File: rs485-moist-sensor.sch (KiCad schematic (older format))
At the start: 26 parts, among them IC1 ATTINY441-MU, P1 CONN_02X03, P2 CONN_01X04, U1 SP3481EN, X1 16MHz

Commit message: Add schematics PDF
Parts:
- R1, R10, R2, R4, R5, R6, R7, R8, R9, TH1: footprint SMD_Packages:SMD-0603_r -> Resistors_SMD:R_0603
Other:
- note added: "Gerai patikrink kojas datasheete:\n* ar geras pinas EXCITATION signalui?\n* ar yra kokių skirtumų tarp USART1 ir USART2?\n"
- note removed: "Gerai patikrink kojas datasheete:\n* kur yra programavimo pinai ir kur spi\n* ar geras pinas EXCITATION signalui?\n* ar yra kokių skirtumų tarp USART1 ir USART2?\n\nBe to:\n* ar lengva rasti 20MHz kristalų?\n* ar darom temperatūros sensorius?"
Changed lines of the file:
@@
 encoding utf-8
 Sheet 1 1
-Title ""
-Date ""
+Title "Digital soil moisture sensor"
+Date "Tue 17 Feb 2015"
 Rev ""
-Comp ""
-Comment1 ""
+Comp "Catnip electronics"
+Comment1 "by Albertas Mickėnas mic@wemakethings.net"
 Comment2 ""
 Comment3 ""
@@
 F 0 "R4" V 8330 3050 50  0000 C CNN
 F 1 "R" V 8257 3051 50  0000 C CNN
-F 2 "SMD_Packages:SMD-0603_r" V 8180 3050 30  0001 C CNN
+F 2 "Resistors_SMD:R_0603" V 8180 3050 30  0001 C CNN
 F 3 "" H 8250 3050 30  0000 C CNN
 	1    8250 3050
@@
 F 0 "R5" V 9380 2100 50  0000 C CNN
 F 1 "1M" V 9307 2101 50  0000 C CNN
-F 2 "SMD_Packages:SMD-0603_r" V 9230 2100 30  0001 C CNN
+F 2 "Resistors_SMD:R_0603" V 9230 2100 30  0001 C CNN
 F 3 "" H 9300 2100 30  0000 C CNN
 	1    9300 2100
@@
 F 0 "R8" V 9680 4050 50  0000 C CNN
 F 1 "1M" V 9607 4051 50  0000 C CNN
-F 2 "SMD_Packages:SMD-0603_r" V 9530 4050 30  0001 C CNN
+F 2 "Resistors_SMD:R_0603" V 9530 4050 30  0001 C CNN
 F 3 "" H 9600 4050 30  0000 C CNN
 	1    9600 4050
@@
 F 0 "R7" V 9680 2600 50  0000 C CNN
 F 1 "1M" V 9607 2601 50  0000 C CNN
-F 2 "SMD_Packages:SMD-0603_r" V 9530 2600 30  0001 C CNN
+F 2 "Resistors_SMD:R_0603" V 9530 2600 30  0001 C CNN
 F 3 "" H 9600 2600 30  0000 C CNN
 	1    9600 2600
@@
 F 0 "R6" V 9380 3550 50  0000 C CNN
 F 1 "1M" V 9307 3551 50  0000 C CNN
-F 2 "SMD_Packages:SMD-0603_r" V 9230 3550 30  0001 C CNN
+F 2 "Resistors_SMD:R_0603" V 9230 3550 30  0001 C CNN
 F 3 "" H 9300 3550 30  0000 C CNN
 	1    9300 3550
@@
 F 0 "R1" V 4730 2900 50  0000 C CNN
 F 1 "10k" V 4657 2901 50  0000 C CNN
-F 2 "SMD_Packages:SMD-0603_r" V 4580 2900 30  0001 C CNN
+F 2 "Resistors_SMD:R_0603" V 4580 2900 30  0001 C CNN
 F 3 "" H 4650 2900 30  0000 C CNN
 	1    4650 2900
@@
 SENSE_LOW
 Text Notes 2450 4900 0    60   ~ 0
-Gerai patikrink kojas datasheete:\n* kur yra programavimo pinai ir kur spi\n* ar geras pinas EXCITATION signalui?\n* ar yra kokių skirtumų tarp USART1 ir USART2?\n\nBe to:\n* ar lengva rasti 20MHz kristalų?\n* ar darom temperatūros sensorius?
+Gerai patikrink kojas datasheete:\n* ar geras pinas EXCITATION signalui?\n* ar yra kokių skirtumų tarp USART1 ir USART2?\n
 $Comp
 L THERMISTOR TH1
@@
 F 0 "TH1" V 7350 4600 50  0000 C CNN
 F 1 "THERMISTOR" V 7150 4550 50  0000 C BNN
-F 2 "SMD_Packages:SMD-0603_r" H 7250 4550 60  0001 C CNN
+F 2 "Resistors_SMD:R_0603" H 7250 4550 60  0001 C CNN
 F 3 "" H 7250 4550 60  0000 C CNN
 	1    7250 4550
@@
 F 0 "R2" V 7330 4050 50  0000 C CNN
 F 1 "10k 0.1%" V 7257 4051 50  0000 C CNN
-F 2 "SMD_Packages:SMD-0603_r" V 7180 4050 30  0001 C CNN
+F 2 "Resistors_SMD:R_0603" V 7180 4050 30  0001 C CNN
 F 3 "" H 7250 4050 30  0000 C CNN
 	1    7250 4050
@@
 F 0 "R9" V 5630 2300 50  0000 C CNN
 F 1 "1k" V 5557 2301 50  0000 C CNN
-F 2 "SMD_Packages:SMD-0603_r" V 5480 2300 30  0001 C CNN
+F 2 "Resistors_SMD:R_0603" V 5480 2300 30  0001 C CNN
 F 3 "" H 5550 2300 30  0000 C CNN
 	1    5550 2300
@@
 F 0 "R10" V 7530 1900 50  0000 C CNN
 F 1 "120" V 7457 1901 50  0000 C CNN
-F 2 "SMD_Packages:SMD-0603_r" V 7380 1900 30  0001 C CNN
+F 2 "Resistors_SMD:R_0603" V 7380 1900 30  0001 C CNN
 F 3 "" H 7450 1900 30  0000 C CNN
 	1    7450 1900

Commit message: Some most recent changes
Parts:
- D1, D2: value DIODESCH -> BAT54
- R4: value R -> 330
- R9: value 1k -> 330
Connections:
- wire segments 42 -> 40
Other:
- moved on the sheet: C1, C2, C3, C4, C5, C6, C7, R10, R2, R4, R5, R6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

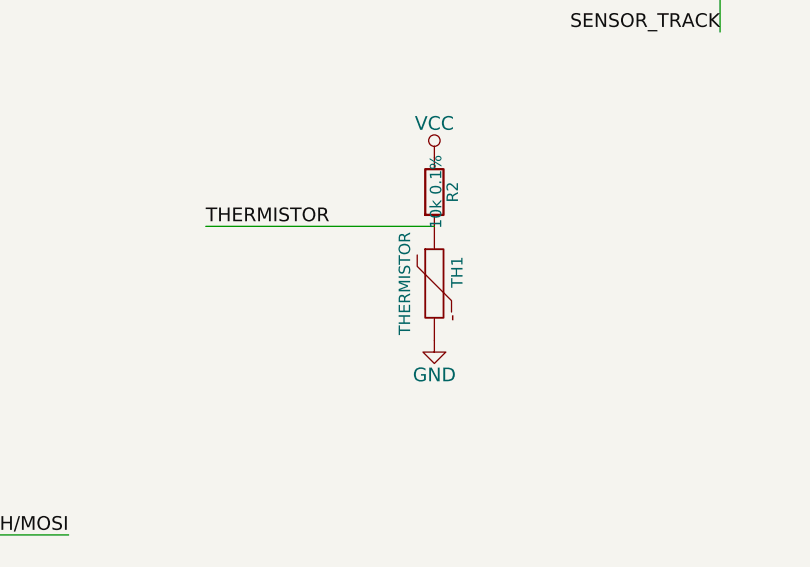
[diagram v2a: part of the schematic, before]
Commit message: Specify thermistor
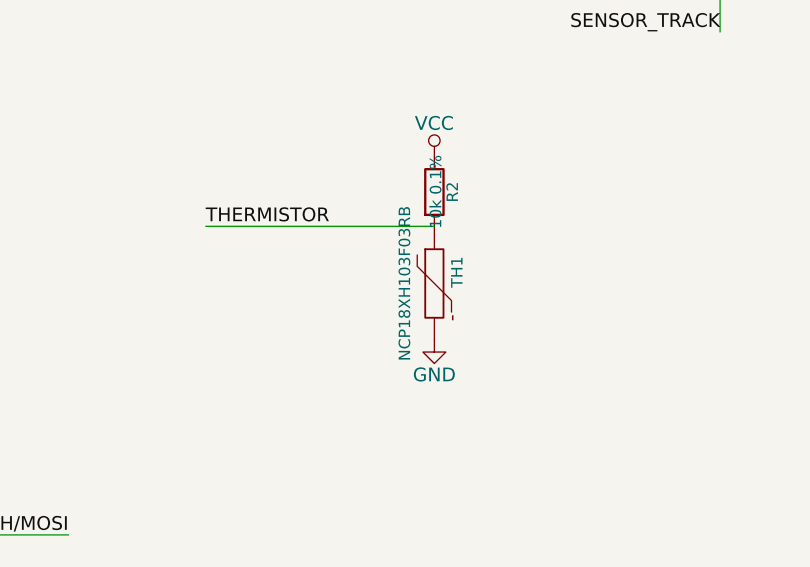
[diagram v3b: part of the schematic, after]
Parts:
- TH1: value THERMISTOR -> NCP18XH103F03RB
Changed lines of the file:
@@
 P 7250 4550
 F 0 "TH1" V 7350 4600 50  0000 C CNN
-F 1 "THERMISTOR" V 7150 4550 50  0000 C BNN
+F 1 "NCP18XH103F03RB" V 7150 4550 50  0000 C BNN
 F 2 "Resistors_SMD:R_0603" H 7250 4550 60  0001 C CNN
 F 3 "" H 7250 4550 60  0000 C CNN

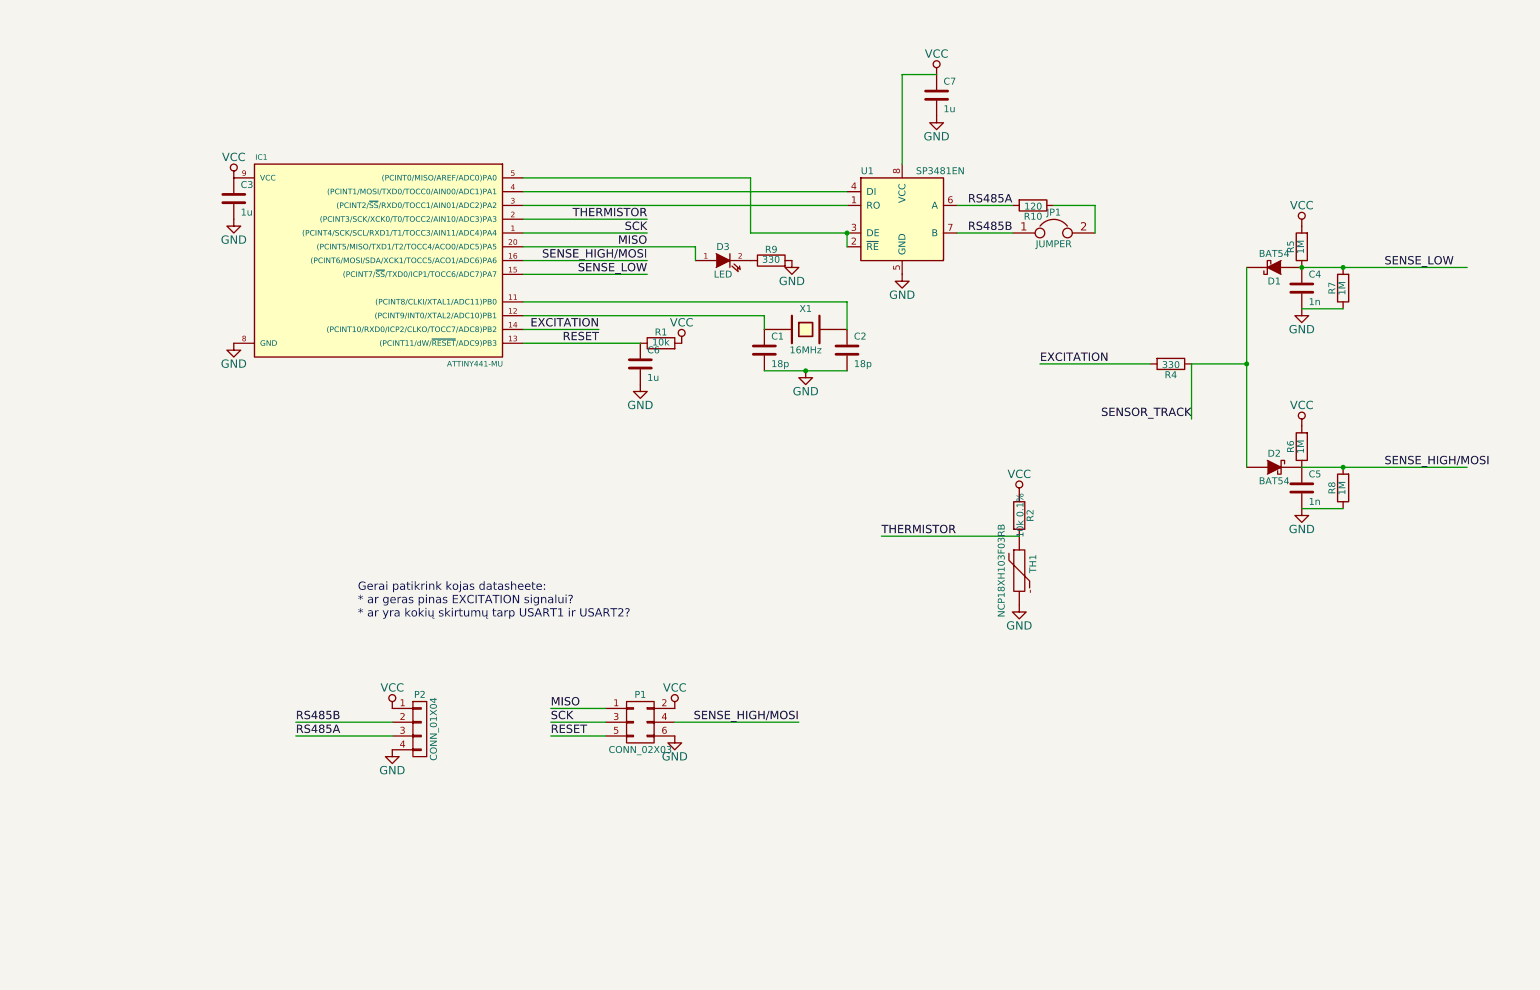
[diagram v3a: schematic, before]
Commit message: Add a local voltage regulator, add antistatic protection, specify transceiver, change attiny441 package to soic-14, route everything
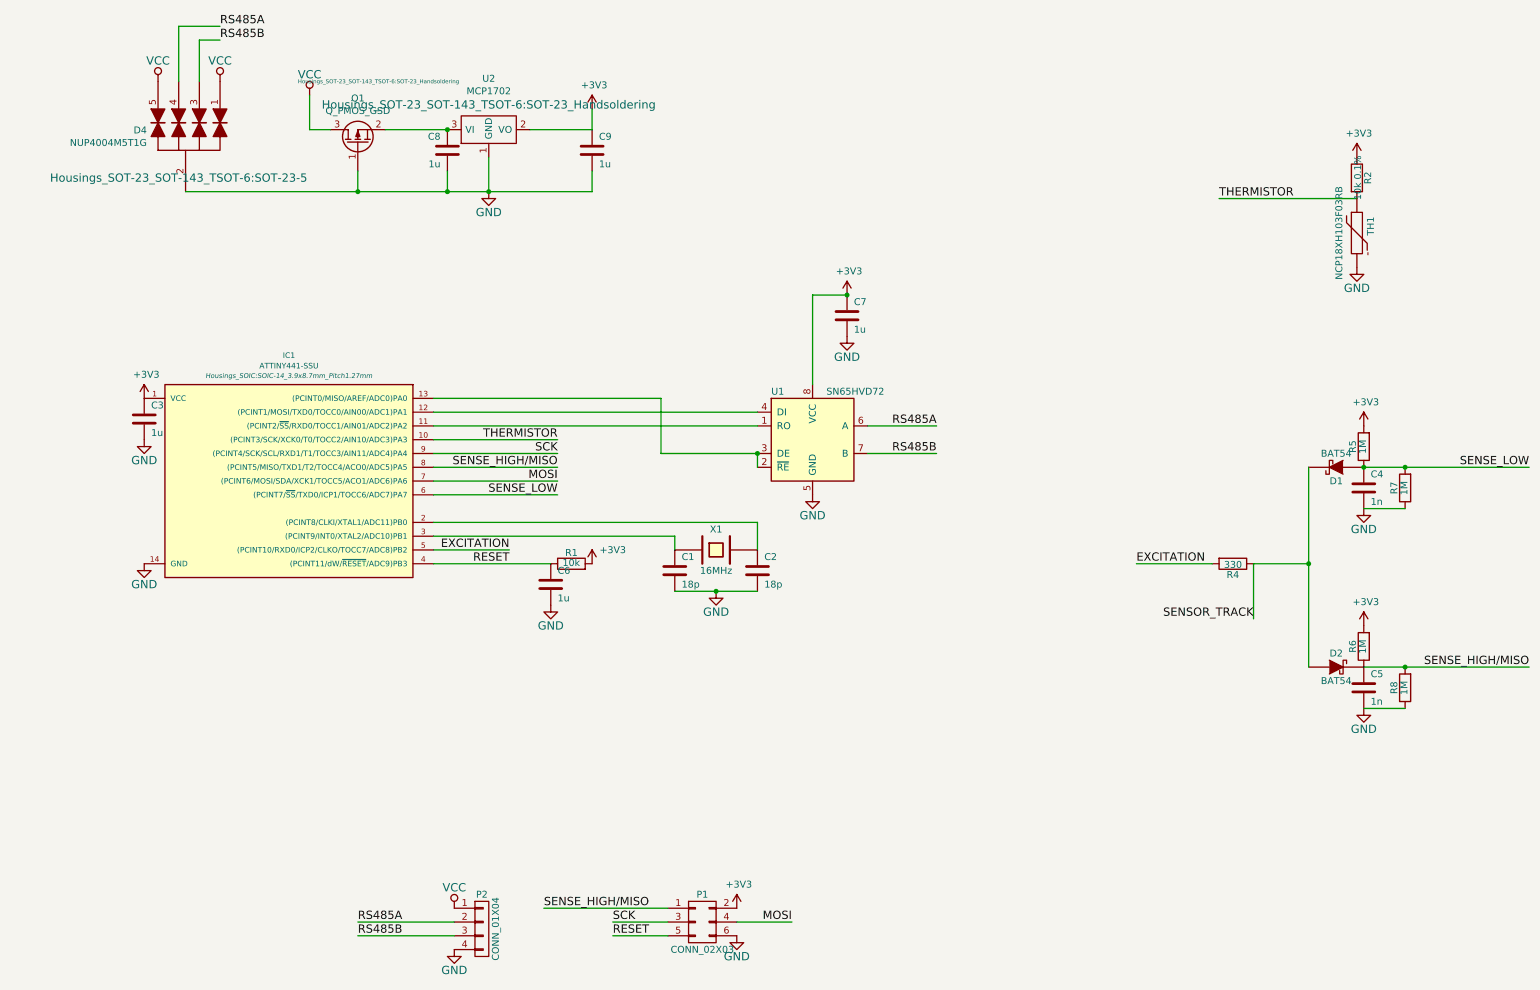
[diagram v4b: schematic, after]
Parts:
- removed D3: LED, LEDs:LED-0603, symbol LED
- removed IC1: ATTINY441-MU, Housings_DFN_QFN:QFN-20-1EP_4x4mm_Pitch0.5mm, symbol ATTINY441-MU
- removed JP1: JUMPER, SMD_Packages:SMD-0603_r, symbol JUMPER
- removed R10: 120, Resistors_SMD:R_0603, symbol R
- removed R9: 330, Resistors_SMD:R_0603, symbol R
- added C8, C9: 1u, Capacitors_SMD:C_0603, symbol C
- added D4: NUP4004M5T1G, Housings_SOT-23_SOT-143_TSOT-6:SOT-23-5, symbol TVS-ARRAY
- added IC1: ATTINY441-SSU, Housings_SOIC:SOIC-14_3.9x8.7mm_Pitch1.27mm, symbol ATTINY441-SSU
- added Q1: Q_PMOS_GSD, Housings_SOT-23_SOT-143_TSOT-6:SOT-23_Handsoldering, symbol Q_PMOS_GSD
- added U2: MCP1702, Housings_SOT-23_SOT-143_TSOT-6:SOT-23_Handsoldering, symbol MCP1702
- P2: footprint Pin_Headers:Pin_Header_Straight_1x04 -> Pin_Headers:Pin_Header_Straight_1x04_Pitch2.54mm; Distributor (none) -> ?; Manufacturer (none) -> ?; PartNo (none) -> ?
- U1: value SP3481EN -> SN65HVD72; Distributor (none) -> 2542747; Manufacturer (none) -> TEXAS INSTRUMENTS; PartNo (none) -> SN65HVD72DR
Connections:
- net labels added: +3V3, MOSI, SENSE_HIGH/MISO
- net labels removed: MISO, SENSE_HIGH/MOSI
- wire segments 40 -> 51
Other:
- note removed: "Gerai patikrink kojas datasheete:\n* ar geras pinas EXCITATION signalui?\n* ar yra kokių skirtumų tarp USART1 ir USART2?\n"
- moved on the sheet: C1, C2, C3, C4, C5, C6, C7, D1, D2, P1, P2, R1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

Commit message: Another board spin - add 3.3v regulator, other rs485 transceiver, esd protection
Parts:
- Q1: symbol Q_PMOS_GSD -> Q_PMOS_GSD-RESCUE-rs485-moist-sensor
- U1: symbol SP3481EN -> SP3481EN-RESCUE-rs485-moist-sensor
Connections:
- net RX: now reaches IC1.11 ((PCINT2/~SS~/RXD0/TOCC1/AIN01/ADC2)PA2), U1.1 (RO)
- net RS485_FLOW_CTRL: now reaches IC1.13 ((PCINT0/MISO/AREF/ADC0)PA0), U1.2 (~RE~), U1.3 (DE)
- net TX: now reaches IC1.12 ((PCINT1/MOSI/TXD0/TOCC0/AIN00/ADC1)PA1), U1.4 (DI)
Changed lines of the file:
@@
 EESchema Schematic File Version 2
+LIBS:rs485-moist-sensor-rescue
 LIBS:power
 LIBS:device
@@
 $EndComp
 $Comp
-L SP3481EN U1
+L SP3481EN-RESCUE-rs485-moist-sensor U1
 U 1 1 54DF0ADA
 P 5750 3600
@@
 $EndComp
 $Comp
-L Q_PMOS_GSD Q1
+L Q_PMOS_GSD-RESCUE-rs485-moist-sensor Q1
 U 1 1 5894816E
 P 2450 1450
@@
 	1    0    0    -1
 $EndComp
+Text Label 3900 3400 2    60   ~ 0
+TX
+Text Label 3900 3500 2    60   ~ 0
+RX
+Text Label 3900 3300 2    60   ~ 0
+RS485_FLOW_CTRL
 $EndSCHEMATC

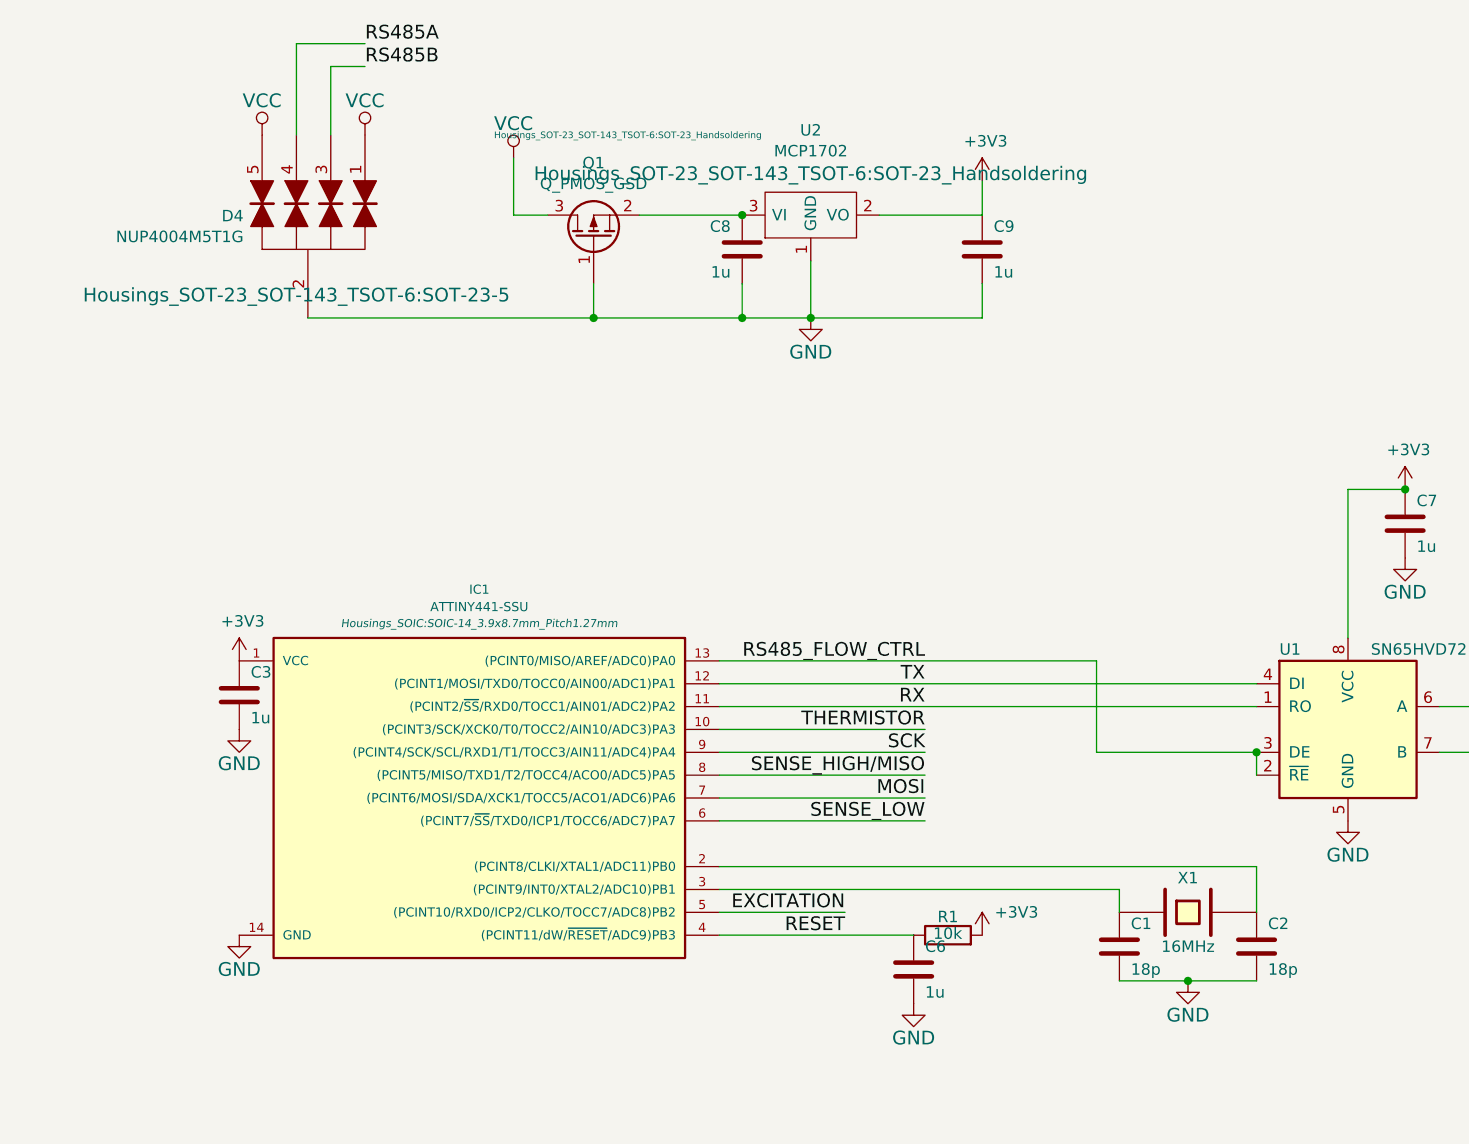
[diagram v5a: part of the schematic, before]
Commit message: Add part numbers and Farnell order numbers to the mail components
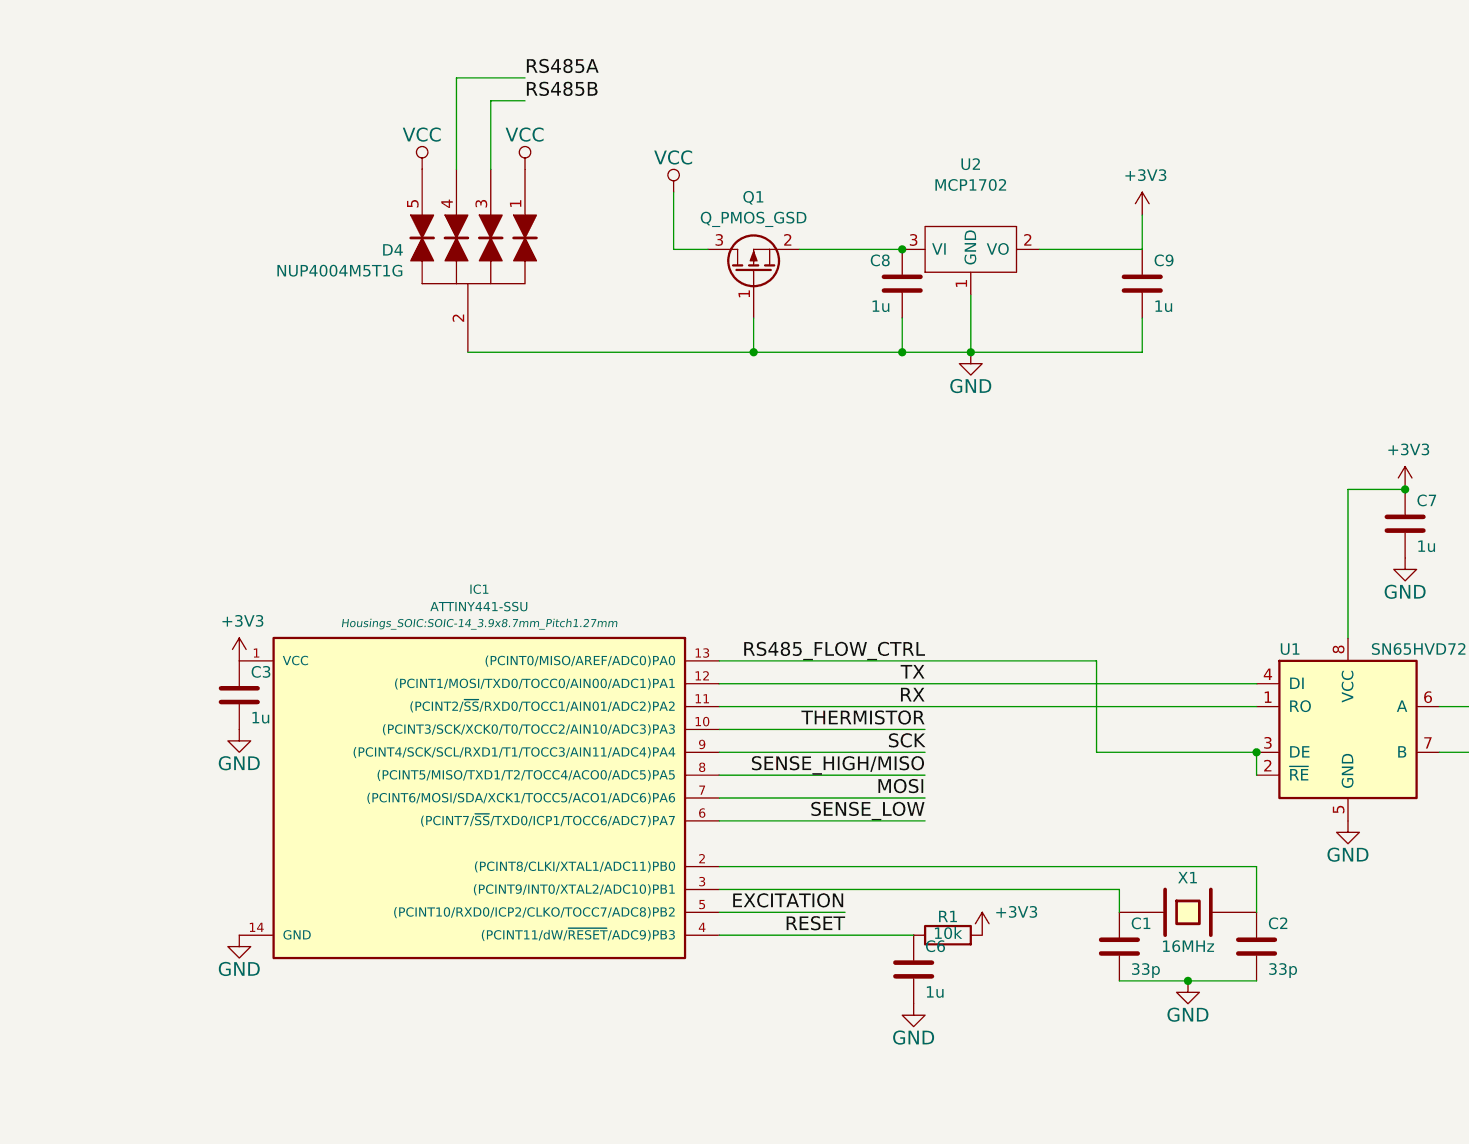
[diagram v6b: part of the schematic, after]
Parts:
- C1, C2: value 18p -> 33p; Distributor (none) -> 2310585; Manufacturer (none) -> MULTICOMP; PartNo (none) -> MC0603N330J500CT
- D1, D2: Distributor (none) -> 2575121; Manufacturer (none) -> NEXPERIA; PartNo (none) -> RB751S40
- IC1: Distributor ? -> 2396717; Manufacturer ? -> MICROCHIP; PartNo ? -> ATTINY441-SSU
- Q1: Distributor ? -> 1894738; Manufacturer ? -> NXP; PartNo ? -> NX2301P
- R2: Distributor (none) -> 2379939; Manufacturer (none) -> PANASONIC ELECTRONIC COMPONENTS; PartNo (none) -> ERJ3RBD1002V
- TH1: Distributor (none) -> 2456122; Manufacturer (none) -> MURATA; PartNo (none) -> NCP18XH103F03RB
- U2: Distributor ? -> 1331490; Manufacturer ? -> MICROCHIP; PartNo ? -> MCP1702T-3302E/CB
- X1: Distributor (none) -> 2395958; Manufacturer (none) -> MULTICOMP; PartNo (none) -> MCRSD16000F183000RR
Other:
- moved on the sheet: C8, C9, D4, Q1, U2
